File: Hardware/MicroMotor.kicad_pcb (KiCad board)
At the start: 4 copper layers, 76.9 x 39.5 mm, 109 parts, among them J1 USB_B_Micro, J2 Conn_01x04_Male, J3 Conn_01x05_Male, J4 Conn_01x02_Female, J5 Conn_01x11_Female, J8 Conn_01x01_Male, Q1 CSD18537NQ5A, Q2 CSD18537NQ5A, Q3 CSD18537NQ5A, Q4 CSD18537NQ5A, Q5 CSD18537NQ5A, Q6 CSD18537NQ5A, SW1 SW_Push, U1 FT230XQ-T, U10 LP2985-3.3, U11 NC7WZ04, U2 STM32F410RBTx, U3 ACSL-6210-00RE, U4 SN74CB3Q3253RGYR, U5 SN74CB3Q3253RGYR, U6 SN74CB3Q3253RGYR, U7 LM2940IMP-10_NOPB, U8 LMR14203, U9 HIP4086ABZ

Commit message: Began mux remove and part consolidation
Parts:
- removed C11, C12, C13: 0.1uF, Capacitor_SMD:C_0603_1608Metric
- removed G***: LOGO, kyleRhess_logos:muMotor_logo
- removed G***: LOGO, kyleRhess_logos:11082020
- removed G***: LOGO, kyleRhess_logos:403a183
- removed G***: LOGO, kyleRhess_logos:kylerhess_github
- removed G***: LOGO, kyleRhess_logos:rev_0p1
- removed G***: LOGO, kyleRhess_logos:logo_foxhound
- removed G***: LOGO, kyleRhess_logos:logo_blackmesa
- removed J8 (x4): Conn_01x01_Male, Connector_Pin:Pin_D0.5mm_L6.5mm_W1.8mm_FlatFork
- removed REF**: KiCad-Logo2_5mm_Copper, Symbol:KiCad-Logo2_5mm_Copper
- removed REF** (x3): TestPoint_THTPad_D1.0mm_Drill0.5mm, TestPoint:TestPoint_THTPad_D1.0mm_Drill0.5mm
- removed REF**: WEEE-Logo_4.2x6mm_SilkScreen, Symbol:WEEE-Logo_4.2x6mm_SilkScreen
- removed U4, U5, U6: SN74CB3Q3253RGYR, kyleRhess_packages:SN74CB3Q3253RGYR
- added R26: 5.1k, Resistor_SMD:R_0603_1608Metric, F.Cu at (181.2, 80.6)
- added R27: 5.1k, Resistor_SMD:R_0603_1608Metric, F.Cu at (182.8, 80.6)
- added R28: 10k, Resistor_SMD:R_0603_1608Metric, F.Cu at (195.6, 75.8)
- added R29: 10k, Resistor_SMD:R_0603_1608Metric, F.Cu at (154.0, 59.7)
- added R30: 10k, Resistor_SMD:R_0603_1608Metric, F.Cu at (160.1, 57.9)
- J1: value USB_B_Micro -> USB_C_Receptacle_USB2.0; footprint Connector_USB:USB_Micro-B_Molex_47346-0001 -> kyleRhess_packages:USB_C_1054500101
- moved C1 9.53 mm to (172.4, 79.6), turned to 180 degrees
- moved FB1 3.43 mm to (182.7, 85.8)
- moved C2 0.40 mm to (179.6, 80.6)
- moved R1 0.40 mm to (178.0, 80.6)
- moved R2 0.40 mm to (176.4, 80.6)
- moved C3 0.40 mm to (174.8, 80.6)
- moved J1 0.25 mm to (177.3, 73.9)
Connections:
- C1 pad 1: Net-(C1-Pad1) -> /VBUS
- FB1 pad 2: Net-(C1-Pad1) -> /VBUS
- U2 pad 23: Net-(U2-Pad23) -> AHI
- U2 pad 26: Net-(U2-Pad26) -> BHI
- U2 pad 27: Net-(U2-Pad27) -> CHI
- U2 pad 41: -PWM -> ALI
- U2 pad 42: +PWM -> BLI
- U2 pad 43: Net-(U2-Pad43) -> CLI
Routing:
- net ALI: track 9.13 -> 64.2 mm, vias 0 -> 5
- net -PWM: track 55.1 -> 0.00 mm, vias 5 -> 0
- net BLI: track 9.47 -> 55.6 mm, vias 0 -> 6
- net +PWM: track 46.2 -> 0.00 mm, vias 6 -> 0
- net Net-(J1-Pad6): track 12.6 -> 0.00 mm
- net Net-(C1-Pad1): track 7.84 -> 0.00 mm
- net Net-(C2-Pad1): track 6.04 -> 1.55 mm
- net Net-(C3-Pad1): track 5.99 -> 1.55 mm
- net GNDS: track 13.7 -> 16.2 mm, vias 6 -> 5
- net Net-(FB1-Pad1): track 4.85 -> 3.11 mm
- net /VBUS: track 0.00 -> 0.74 mm, vias 0 -> 1
- added copper zone on In2.Cu, net /VBUS

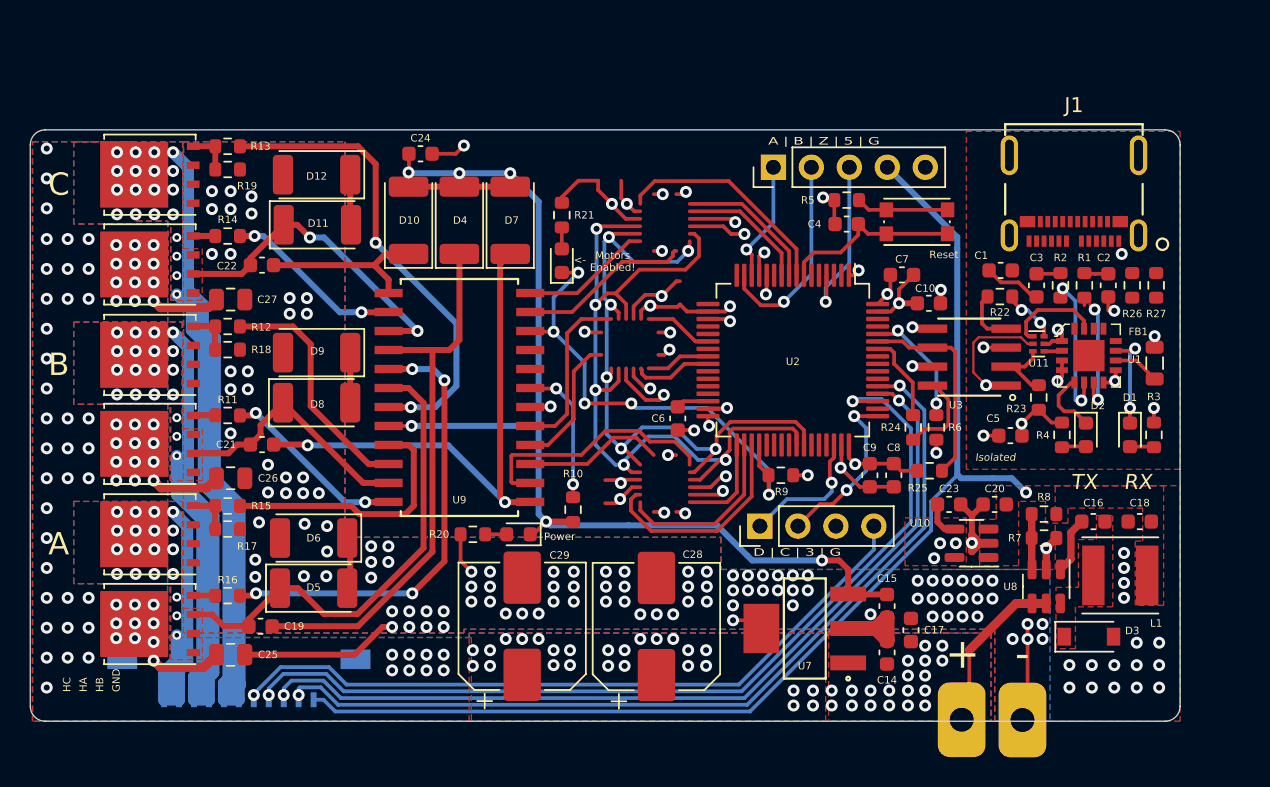
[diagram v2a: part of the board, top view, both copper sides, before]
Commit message: Began making changes for 48V version.
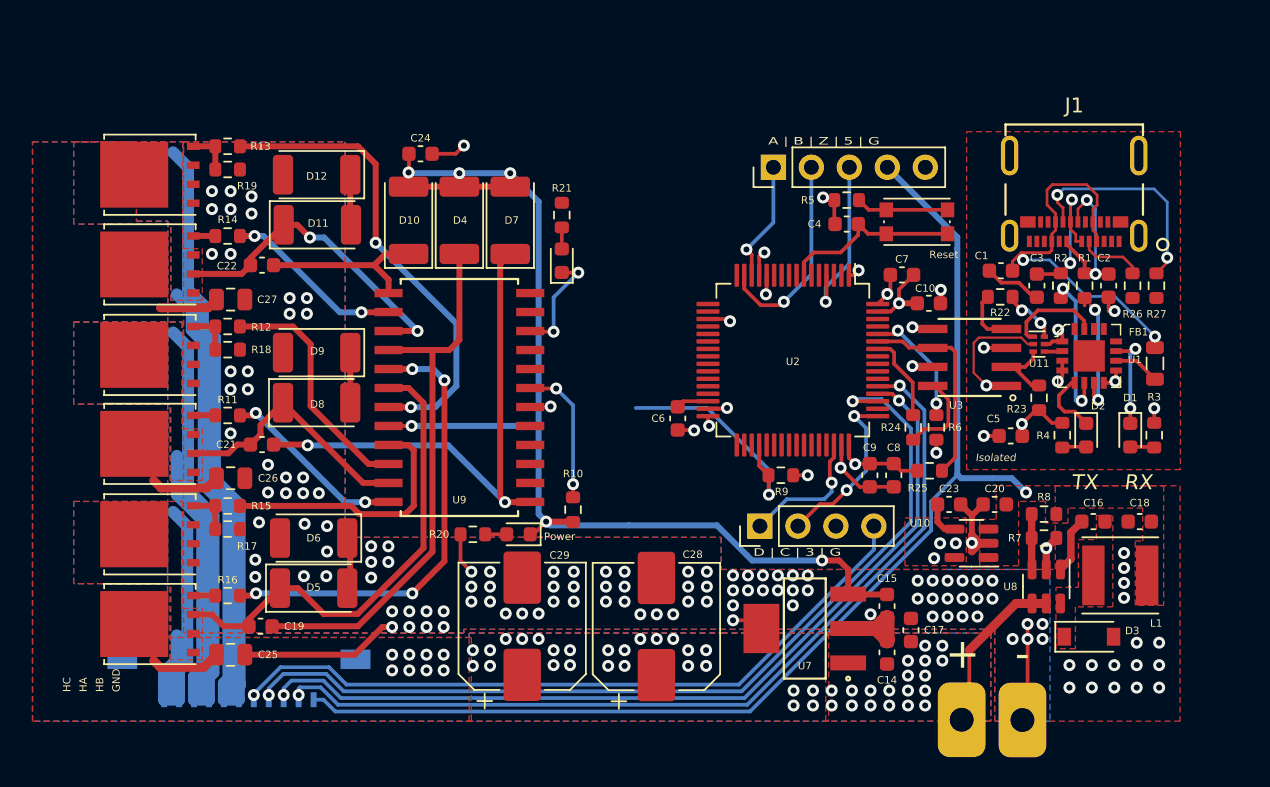
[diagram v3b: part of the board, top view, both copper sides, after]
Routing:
- net ALI: track 64.2 -> 0.00 mm, vias 5 -> 0
- net BLI: track 55.6 -> 0.00 mm, vias 6 -> 0
- net +3V3: track 43.9 -> 16.1 mm, vias 21 -> 12
- net /VBUS: track 0.74 -> 27.5 mm, vias 1 -> 2
- net GND: track 142.1 -> 117.7 mm, vias 154 -> 141
- net BHI: track 16.9 -> 0.00 mm
- net S_1: track 15.0 -> 0.00 mm
- net Net-(J1-PadB5): track 0.00 -> 14.9 mm, vias 0 -> 2
- net S_4: track 14.5 -> 0.00 mm
- net CL_EN: track 12.0 -> 0.00 mm
- net CLI: track 11.6 -> 0.00 mm
- net AHI: track 11.5 -> 0.00 mm
- net Net-(C2-Pad1): track 1.55 -> 11.8 mm, vias 0 -> 2
- net AL_EN: track 9.58 -> 0.00 mm
- net DIS: track 32.4 -> 23.2 mm, vias 5 -> 3
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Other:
- board outline removed
- board text removed: "<-"
- board text removed: "A"
- board text removed: "B"
- board text removed: "C"
- board text removed: "Motors Enabled!"

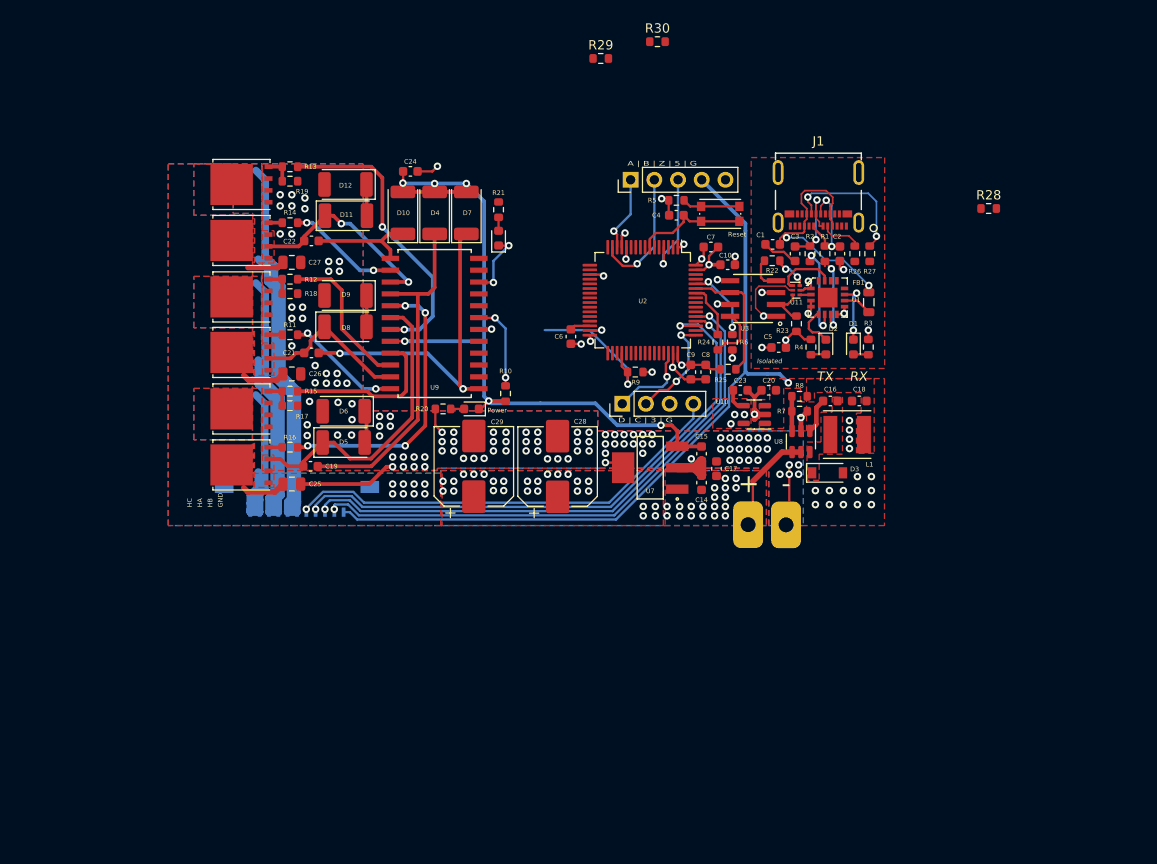
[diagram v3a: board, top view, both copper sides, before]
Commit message: Nearly finished board and schematic changes for FOC and high current.
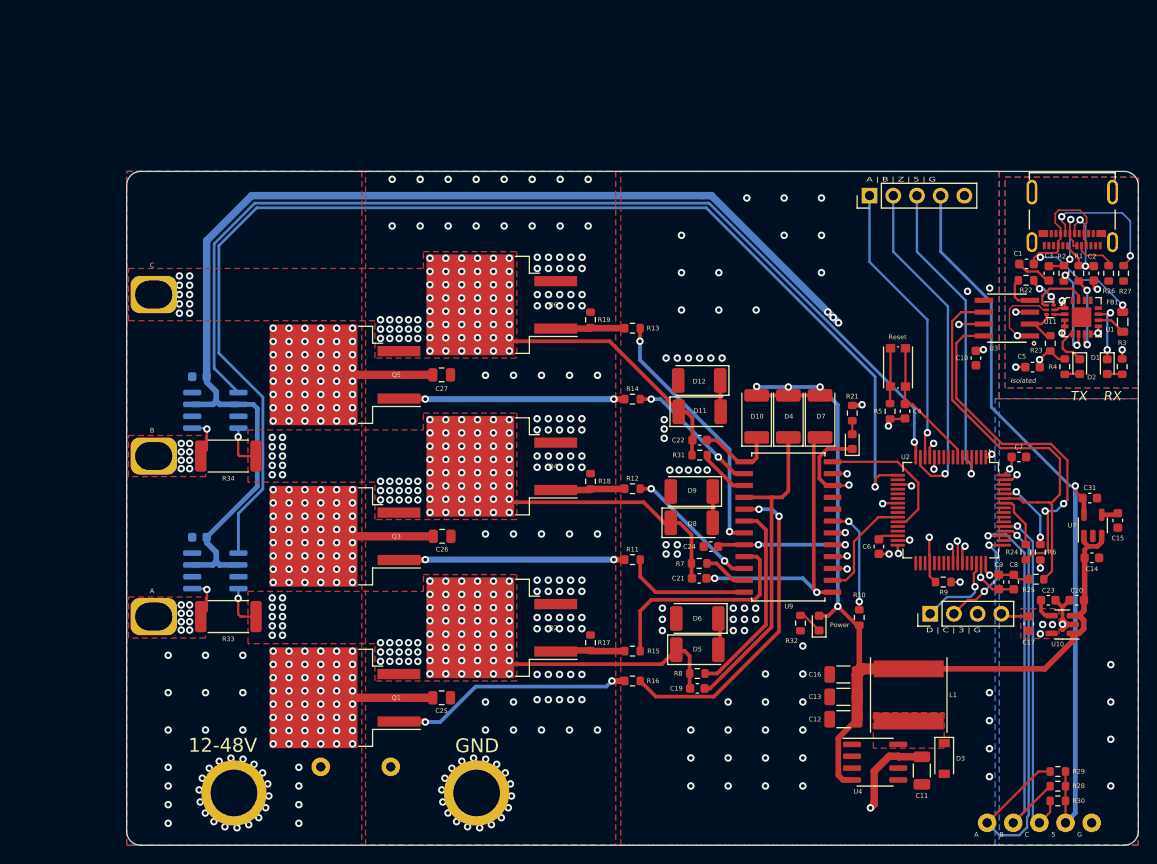
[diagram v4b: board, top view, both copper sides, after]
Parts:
- removed J4: Conn_01x02_Female, digikey-footprints:PinHeader_1x2_P2.54mm
- removed J5: Conn_01x11_Female, Connector_FFC-FPC:Molex_200528-0110_1x11-1MP_P1.00mm_Horizontal
- removed R20: 10k, Resistor_SMD:R_0603_1608Metric
- removed U8: LMR14203, Package_TO_SOT_SMD:TSOT-23-6
- added 12-48V: TestPoint_THTPad_D4.0mm_Drill2.0mm, TestPoint:TestPoint_THTPad_D4.0mm_Drill2.0mm, F.Cu at (110.3, 139.4)
- added 5: TestPoint_Loop_D2.50mm_Drill1.0mm, TestPoint:TestPoint_Loop_D2.50mm_Drill1.0mm, F.Cu at (203.8, 141.6)
- added A: TestPoint_Plated_Hole_D3.0mm, TestPoint:TestPoint_Plated_Hole_D3.0mm, F.Cu at (105.9, 119.9)
- added A: TestPoint_Loop_D2.50mm_Drill1.0mm, TestPoint:TestPoint_Loop_D2.50mm_Drill1.0mm, F.Cu at (195.4, 141.6)
- added B: TestPoint_Plated_Hole_D3.0mm, TestPoint:TestPoint_Plated_Hole_D3.0mm, F.Cu at (105.9, 102.7)
- added B: TestPoint_Loop_D2.50mm_Drill1.0mm, TestPoint:TestPoint_Loop_D2.50mm_Drill1.0mm, F.Cu at (198.2, 141.6)
- added C: TestPoint_Plated_Hole_D3.0mm, TestPoint:TestPoint_Plated_Hole_D3.0mm, F.Cu at (105.9, 85.4)
- added C: TestPoint_Loop_D2.50mm_Drill1.0mm, TestPoint:TestPoint_Loop_D2.50mm_Drill1.0mm, F.Cu at (201.0, 141.6)
- added C11: 1uF, Capacitor_SMD:C_1206_3216Metric, F.Cu at (188.4, 136.0)
- added C12: 47uF, Capacitor_SMD:C_1206_3216Metric, F.Cu at (180.0, 130.5)
- added C13: 47uF, Capacitor_SMD:C_1206_3216Metric, F.Cu at (180.0, 128.1)
- added C31: 1uF, Capacitor_SMD:C_0603_1608Metric, F.Cu at (206.4, 106.8)
- added G: TestPoint_Loop_D2.50mm_Drill1.0mm, TestPoint:TestPoint_Loop_D2.50mm_Drill1.0mm, F.Cu at (206.6, 141.6)
- added GND: TestPoint_THTPad_D4.0mm_Drill2.0mm, TestPoint:TestPoint_THTPad_D4.0mm_Drill2.0mm, F.Cu at (136.3, 139.4)
- added R31: 1.2, Resistor_SMD:R_0603_1608Metric, F.Cu at (164.6, 102.2)
- added R32: 10k, Resistor_SMD:R_0603_1608Metric, F.Cu at (175.4, 120.2)
- added R33: 750u, Resistor_SMD:R_2512_6332Metric, F.Cu at (114.1, 119.5)
- added R34: 750u, Resistor_SMD:R_2512_6332Metric, F.Cu at (114.1, 102.3)
- added U4: LM2594HVM-12, Package_SO:SOIC-8_3.9x4.9mm_P1.27mm, F.Cu at (183.4, 135.1)
- added U5: INA240A3D, Package_SO:SOIC-8_3.9x4.9mm_P1.27mm, B.Cu at (112.7, 114.6)
- added U6: INA240A3D, Package_SO:SOIC-8_3.9x4.9mm_P1.27mm, B.Cu at (112.7, 97.4)
- C14: value 0.47uF -> 1uF
- C15: value 22uF -> 10nF
- C16: value 0.15uF -> 47uF; footprint Capacitor_SMD:C_0603_1608Metric -> Capacitor_SMD:C_1206_3216Metric
- C17: value 2.2uF -> 1uF
- C18: value 47uF -> 0.1uF; moved to B.Cu
- C28: value 220uF 50V -> 1000uF; footprint Capacitor_SMD:CP_Elec_8x10 -> Capacitor_THT:C_Radial_D18.0mm_H35.5mm_P7.50mm; moved to B.Cu
- C29: value 220uF 50V -> 0.1uF; footprint Capacitor_SMD:CP_Elec_8x10 -> Capacitor_SMD:C_0603_1608Metric; moved to B.Cu
- L1: value 15uH -> 100uH; footprint Inductor_SMD:L_Taiyo-Yuden_NR-50xx -> Inductor_SMD:L_Taiyo-Yuden_NR-80xx
- Q1, Q2, Q3, Q4, Q5, Q6: value CSD18537NQ5A -> FDB075N15A; footprint Package_TO_SOT_SMD:TDSON-8-1 -> Package_TO_SOT_SMD:TO-263-2
- R7: value 1.02k -> 1.2
- R8: value 5.62k -> 1.2
- U7: value LM2940IMP-10_NOPB -> LP2985-5.0; footprint kyleRhess_packages:LM2940IMP-10 -> Package_TO_SOT_SMD:SOT-23-5
- moved R30 92.0 mm to (203.0, 139.2)
- moved R29 90.7 mm to (203.0, 136.1)
- moved C18 70.7 mm to (111.0, 93.8)
- moved R28 62.3 mm to (203.0, 137.7)
- moved C24 51.5 mm to (165.8, 112.0), turned to 180 degrees
- moved C21 48.1 mm to (164.6, 115.4)
- moved U7 47.8 mm to (206.7, 109.7), turned to 90 degrees
- moved C19 47.8 mm to (164.3, 127.2)
- moved C22 46.8 mm to (164.6, 100.6)
- moved R15 46.1 mm to (157.4, 123.2)
- moved C15 45.2 mm to (209.4, 109.2)
- moved R10 44.9 mm to (181.7, 119.6)
- moved R16 44.4 mm to (157.4, 126.4)
- moved D5 43.9 mm to (164.3, 123.0)
- moved D6 43.9 mm to (164.3, 119.7)
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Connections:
- net AL_EN renamed Net-(U2-Pad9)
- net BL_EN renamed Net-(U2-Pad24)
- net CL_EN renamed Net-(U2-Pad34)
- net S_0 renamed Net-(U2-Pad10)
- net S_1 renamed Net-(U2-Pad8)
- net S_2 renamed Net-(U2-Pad25)
- net S_3 renamed Net-(U2-Pad22)
- net S_4 renamed Net-(U2-Pad35)
- net S_5 renamed Net-(U2-Pad33)
- C14 pad 2: +VDC -> 12V_Out
- C15 pad 2: +10V -> Net-(C15-Pad2)
- C16 pad 1: Net-(C16-Pad1) -> GND
- C16 pad 2: Net-(C16-Pad2) -> 12V_Out
- C17 pad 1: +VDC -> GND
- C17 pad 2: GND -> +3V3
- C18 pad 2: 5V_Out -> +3V3
- C20 pad 2: 5V_Out -> 12V_Out
- C24 pad 1: +10V -> 12V_Out
- C25 pad 1: +VDC -> +48V
- C26 pad 1: +VDC -> +48V
- C27 pad 1: +VDC -> +48V
- C28 pad 1: +VDC -> +48V
- C29 pad 1: +VDC -> GND
- C29 pad 2: GND -> +3V3
- D10 pad 2: +10V -> 12V_Out
- D13 pad 1: +10V -> Net-(D13-Pad1)
- D13 pad 2: Net-(D13-Pad2) -> 12V_Out
- D3 pad 1: Net-(C16-Pad1) -> Net-(D3-Pad1)
- D4 pad 2: +10V -> 12V_Out
- D7 pad 2: +10V -> 12V_Out
- L1 pad 1: Net-(C16-Pad1) -> Net-(D3-Pad1)
- L1 pad 2: 5V_Out -> 12V_Out
- Q1 pad 1: MTR_A -> AHO
- Q1 pad 2: MTR_A -> +48V
- Q2 pad 1: GND -> ALO
- Q2 pad 2: GND -> MTR_A
- Q3 pad 1: MTR_B -> BHO
- Q3 pad 2: MTR_B -> +48V
- Q4 pad 1: GND -> BLO
- Q4 pad 2: GND -> MTR_B
- Q5 pad 1: MTR_C -> CHO
- Q5 pad 2: MTR_C -> +48V
- Q6 pad 1: GND -> CLO
- Q6 pad 2: GND -> MTR_C
- R10 pad 1: +10V -> 12V_Out
- R7 pad 1: GND -> Net-(R7-Pad1)
- R7 pad 2: Net-(R7-Pad2) -> MTR_B
- R8 pad 1: Net-(R7-Pad2) -> Net-(R8-Pad1)
- R8 pad 2: 5V_Out -> MTR_A
- U10 pad 1: 5V_Out -> 12V_Out
- U10 pad 3: 5V_Out -> 12V_Out
- U2 pad 16: Net-(U2-Pad16) -> B_SENS
- U2 pad 17: Net-(U2-Pad17) -> A_SENS
- U7 pad 1: +VDC -> 12V_Out
- U7 pad 3: +10V -> 12V_Out
- U7 pad 4: GND -> Net-(C15-Pad2)
- U9 pad 15: MTR_C -> Net-(R31-Pad1)
- U9 pad 18: MTR_A -> Net-(R8-Pad1)
- U9 pad 20: +10V -> 12V_Out
- U9 pad 23: MTR_B -> Net-(R7-Pad1)
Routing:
- net A_SENS: track 0.00 -> 130.7 mm, vias 0 -> 1
- net +3V3: track 16.1 -> 143.5 mm, vias 12 -> 16
- net 12V_Out: track 0.00 -> 117.8 mm, vias 0 -> 5
- net +48V: track 0.00 -> 113.6 mm, vias 0 -> 180
- net B_SENS: track 0.00 -> 108.2 mm, vias 0 -> 1
- net GND: track 117.7 -> 25.9 mm, vias 141 -> 199
- net +10V: track 81.0 -> 0.00 mm, vias 6 -> 0
- net MTR_C: track 91.2 -> 32.9 mm, vias 2 -> 73
- net HALL_C: track 76.7 -> 37.1 mm, vias 2 -> 1
- net HALL_B: track 74.7 -> 41.5 mm, vias 2 -> 1
- net Net-(R24-Pad1): track 5.89 -> 38.1 mm, vias 0 -> 2
- net USART1_RX: track 13.8 -> 45.4 mm
- net HALL_A: track 73.6 -> 47.7 mm, vias 2 -> 1
- net +VDC: track 24.6 -> 0.00 mm, vias 53 -> 0
- net AHO: track 1.48 -> 26.0 mm, vias 0 -> 2
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- added copper zone on F.Cu, net +48V
- added copper zone on In1.Cu, net +48V
- added copper zone on In2.Cu, net +48V
- added copper zone on F.Cu, net A_OUT
- added copper zone on In1.Cu, net A_OUT
- added copper zone on In2.Cu, net A_OUT
- added copper zone on F.Cu, net B_OUT
- added copper zone on In1.Cu, net B_OUT
- added copper zone on In2.Cu, net B_OUT
- added copper zone on B.Cu, net GNDS
- added copper zone on F.Cu, net Net-(D3-Pad1)
- removed copper zone on B.Cu, net +VDC
- removed copper zone on F.Cu, net +VDC
- removed copper zone on In1.Cu, net +VDC
- removed copper zone on In2.Cu, net +VDC
- removed copper zone on F.Cu, net 5V_Out
- removed copper zone on B.Cu, net MTR_A
- removed copper zone on B.Cu, net MTR_B
- removed copper zone on B.Cu, net MTR_C
- removed copper zone on F.Cu, net Net-(C16-Pad1)
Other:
- board outline added: 108.4 x 72.2 mm
- board text removed: "+"
- board text removed: "-"
- board text removed: "GND"
- board text removed: "HA"
- board text removed: "HB"
- board text removed: "HC"
